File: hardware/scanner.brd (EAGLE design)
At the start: 65 x 56 mm, 24 parts, among them K1 PIN20X2, U1 CAT24C32WI-GT3, U2 TPS61165DBV

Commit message: update board layout
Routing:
- net +3V3: track 85.8 -> 63.3 mm
- net GND: track 21.2 -> 18.2 mm, vias 5 -> 6
- net N$1: track 32.3 -> 33.4 mm

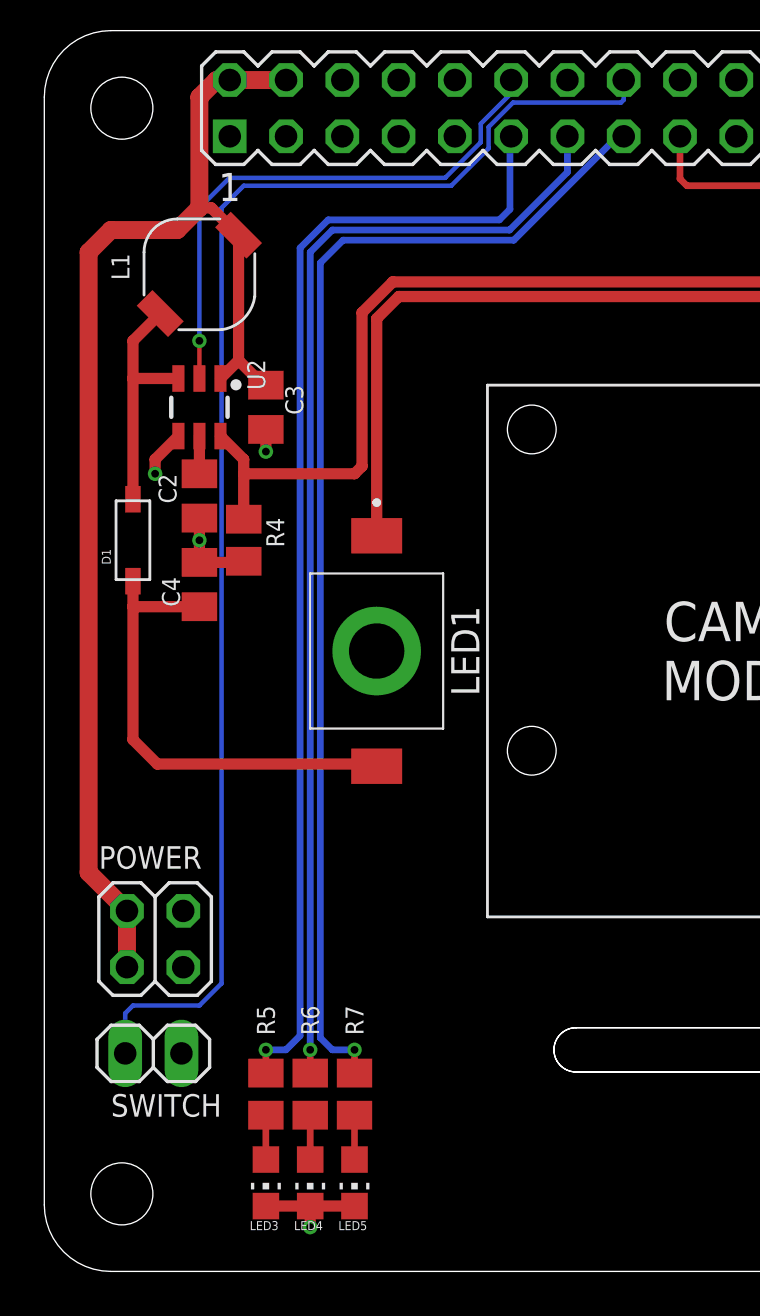
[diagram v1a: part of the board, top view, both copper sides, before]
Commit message: new power connector
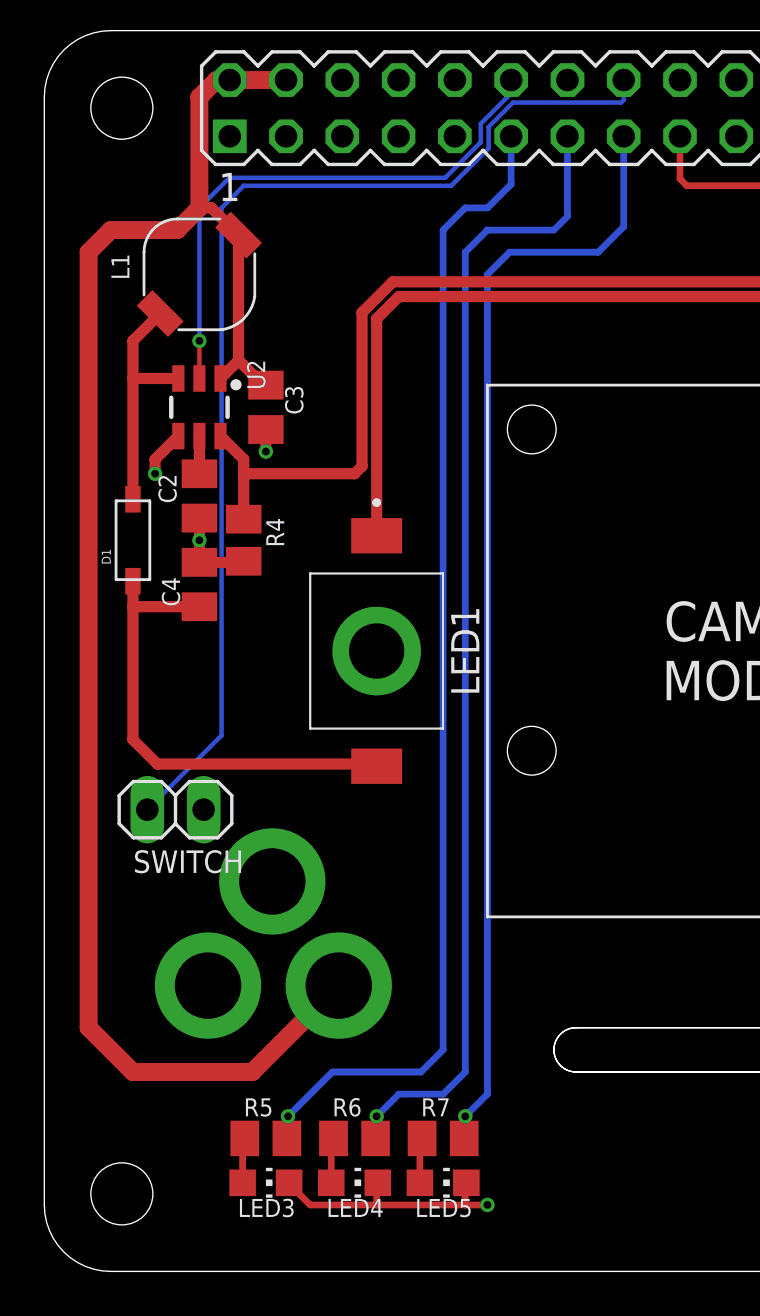
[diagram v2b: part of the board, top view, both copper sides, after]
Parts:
- POWER: value (none) -> 2.1MMJACKTHM; device pinhead:2X02 -> adafruit:PJ-102A
- moved SWITCH 11.0 mm to (5.92, 20.8)
- moved R7 4.47 mm to (18.0, 6.00), turned to 180 degrees
- moved LED5 4.00 mm to (18.0, 4.00), turned to 270 degrees
- moved R6 2.83 mm to (14.0, 6.00), turned to 180 degrees
- moved POWER 2.24 mm to (4.00, 13.0), flipped to the bottom, turned to 270 degrees
- moved LED4 2.00 mm to (14.0, 4.00), turned to 270 degrees
- moved R5 2.00 mm to (10.0, 6.00), turned to 180 degrees
- turned LED3 to 270 degrees
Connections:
- net +5V: now also POWER.TIP; no longer POWER.1, POWER.2
- net GND: now also POWER.RING, POWER.RING_SW; no longer POWER.3, POWER.4
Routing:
- net +5V: track 58.8 -> 74.6 mm
- net N$4: track 63.3 -> 50.2 mm
- net GND: track 18.2 -> 24.7 mm
- net N$20: track 53.9 -> 50.6 mm

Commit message: rename routes
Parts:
- removed SWITCH: (no value), pinhead:1X02
- added TRIGGER: (no value), pinhead:1X02
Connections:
- net N$1 renamed EEPROM_SDA
- net N$16 renamed LED4
- net N$19 renamed LED3
- net N$20 renamed LED5
- net N$3 renamed EEPROM_SCL
- net N$6 renamed EEPROM_WP
- removed net N$4: K1.16, SWITCH.2
- new net TRIGGER: K1.16, TRIGGER.2
- net GND: now also TRIGGER.1; no longer SWITCH.1
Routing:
- net TRIGGER: track 0.00 -> 50.8 mm
- net N$4: track 50.2 -> 0.00 mm
- net N$8: track 78.8 -> 78.1 mm
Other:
- board text added: "shopper.ink © Scanner HAT"
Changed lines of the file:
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@@
 <text x="32.635" y="28" size="1.778" layer="25" align="center">CAMERA
 MODULE</text>
+<text x="63" y="8" size="2.54" layer="25" rot="R90">shopper.ink ©
+Scanner HAT</text>
 </plain>
 <attributes>
@@
 </element>
 <element name="R1" library="resistor" package="M0805" value="3k9" x="61" y="39" smashed="yes" rot="R270">
-<attribute name="NAME" x="61" y="37" size="0.6096" layer="25" ratio="10" rot="R180" align="center"/>
+<attribute name="NAME" x="61" y="37" size="0.8128" layer="25" ratio="10" rot="R180" align="center"/>
 <attribute name="TOLERANCE" value="5%" x="61" y="39" size="1.778" layer="27" rot="R270" display="off"/>
 <attribute name="VALUE" x="59.984" y="37.1585" size="0.8128" layer="27" rot="R270"/>
@@
 </element>
 <element name="R2" library="resistor" package="M0805" value="3k9" x="59" y="39" smashed="yes" rot="R270">
-<attribute name="NAME" x="59" y="37" size="0.6096" layer="25" ratio="10" rot="R180" align="center"/>
+<attribute name="NAME" x="59" y="37" size="0.8128" layer="25" ratio="10" rot="R180" align="center"/>
 <attribute name="TOLERANCE" value="5%" x="59" y="39" size="1.778" layer="27" rot="R270" display="off"/>
 <attribute name="VALUE" x="57.984" y="37.1585" size="0.8128" layer="27" rot="R270"/>
 </element>
 <element name="U2" library="dword1511-pmic-dcdc" package="SOT-23-6" value="TPS61165DBV" x="7" y="39" smashed="yes" rot="R180">
-<attribute name="NAME" x="9.159" y="41.159" size="0.8128" layer="25" font="vector" rot="R270"/>
+<attribute name="NAME" x="5" y="40" size="0.8128" layer="25" font="vector" rot="R270" align="center-left"/>
 <attribute name="VALUE" x="4.2695" y="41.2225" size="0.8128" layer="27" font="vector" rot="R270"/>
 </element>
@@
 </element>
 <element name="R3" library="resistor" package="M0805" value="1k" x="57" y="39" smashed="yes" rot="R90">
-<attribute name="NAME" x="57" y="37" size="0.6096" layer="25" rot="R180" align="center"/>
+<attribute name="NAME" x="57" y="37" size="0.8128" layer="25" rot="R180" align="center"/>
 <attribute name="TOLERANCE" value="5%" x="57" y="39" size="1.778" layer="27" rot="R90" display="off"/>
 <attribute name="VALUE" x="59.286" y="37.984" size="1.27" layer="27" rot="R90"/>
 </element>
-<element name="SWITCH" library="pinhead" library_urn="urn:adsk.eagle:library:325" package="1X02" package3d_urn="urn:adsk.eagle:package:22435/2" value="" x="5.92" y="20.84" smashed="yes" rot="R180">
-<attribute name="NAME" x="9" y="19" size="1.016" layer="25" ratio="10" rot="R180"/>
-<attribute name="VALUE" x="8.46" y="24.015" size="1.27" layer="27" rot="R180"/>
+<element name="TRIGGER" library="pinhead" library_urn="urn:adsk.eagle:library:325" package="1X02" package3d_urn="urn:adsk.eagle:package:22435/2" value="" x="5.65" y="20.315" smashed="yes" rot="R180">
+<attribute name="NAME" x="8.73" y="18.475" size="1.016" layer="25" ratio="10" rot="R180"/>
+<attribute name="VALUE" x="8.19" y="23.49" size="1.27" layer="27" rot="R180"/>
 </element>
 <element name="JP1" library="pinhead" library_urn="urn:adsk.eagle:library:325" package="1X02" package3d_urn="urn:adsk.eagle:package:22435/2" value="" x="59" y="35" smashed="yes">
@@
 </element>
 <element name="D1" library="adafruit" library_urn="urn:adsk.eagle:library:420" package="SOD-123" package3d_urn="urn:adsk.eagle:package:6240753/1" value="40V 550mA" x="4" y="33" smashed="yes" rot="R90">
-<attribute name="NAME" x="3" y="31.9" size="0.4064" layer="25" rot="R90"/>
+<attribute name="NAME" x="3" y="31.9" size="0.8128" layer="25" rot="R90"/>
 <attribute name="VALUE" x="5.284" y="31.9" size="0.4064" layer="27" rot="R90"/>
 </element>
@@
 <contactref element="U1" pad="1"/>
 <contactref element="U1" pad="2"/>
-<contactref element="SWITCH" pad="1"/>
+<contactref element="TRIGGER" pad="1"/>
 <contactref element="JP1" pad="2"/>
 <polygon width="0.1524" layer="2">
@@
 <wire x1="8.37" y1="51.23" x2="28.69" y2="51.23" width="0" layer="19" extent="1-1"/>
 </signal>
-<signal name="N$1">
+<signal name="EEPROM_SDA">
 <contactref element="R1" pad="1"/>
 <contactref element="K1" pad="28"/>
@@
 <wire x1="2" y1="11" x2="2" y2="46" width="0.8128" layer="1"/>
 </signal>
-<signal name="N$4">
+<signal name="TRIGGER">
 <contactref element="K1" pad="16"/>
-<contactref element="SWITCH" pad="2"/>
+<contactref element="TRIGGER" pad="2"/>
 <wire x1="8" y1="48" x2="9" y2="49" width="0.2032" layer="16"/>
 <wire x1="9" y1="49" x2="18.365" y2="49" width="0.2032" layer="16"/>
@@
 <wire x1="20.054" y1="51.65084375" x2="21.15715625" y2="52.754" width="0.2032" layer="16"/>
 <wire x1="21.15715625" y1="52.754" x2="26.03084375" y2="52.754" width="0.2032" layer="16"/>
-<wire x1="4.65" y1="20.84" x2="8" y2="24.19" width="0.2032" layer="16"/>
-<wire x1="8" y1="24.19" x2="8" y2="48" width="0.2032" layer="16"/>
+<wire x1="4.38" y1="20.315" x2="8" y2="23.935" width="0.2032" layer="16"/>
+<wire x1="8" y1="23.935" x2="8" y2="48" width="0.2032" layer="16"/>
 </signal>
 <signal name="N$5">
@@
 <wire x1="8.3556" y1="49.3556" x2="18.09244375" y2="49.3556" width="0.2032" layer="16"/>
 </signal>
-<signal name="N$6">
+<signal name="EEPROM_WP">
 <contactref element="U1" pad="7"/>
 <contactref element="JP1" pad="1"/>
@@
 <via x="58" y="42" extent="1-16" drill="0.35"/>
 </signal>
-<signal name="N$3">
+<signal name="EEPROM_SCL">
 <contactref element="R2" pad="1"/>
 <contactref element="U1" pad="6"/>
@@
 <contactref element="LED2" pad="1"/>
 <wire x1="7.95" y1="37.6999" x2="8" y2="37.6499" width="0.508" layer="1"/>
+<wire x1="9" y1="36.6499" x2="9" y2="36" width="0.508" layer="1"/>
 <wire x1="9" y1="36" x2="9" y2="33.95" width="0.508" layer="1"/>
-<wire x1="9" y1="36" x2="14" y2="36" width="0.508" layer="1"/>
-<wire x1="14" y1="36" x2="14.3396" y2="36.3396" width="0.508" layer="1"/>
-<wire x1="15.72645" y1="44.6604" x2="49.27355" y2="44.6604" width="0.508" layer="1"/>
-<wire x1="14.3396" y1="36.3396" x2="14.3396" y2="43.27355" width="0.508" layer="1"/>
-<wire x1="14.3396" y1="43.27355" x2="15.72645" y2="44.6604" width="0.508" layer="1"/>
-<wire x1="49.27355" y1="44.6604" x2="50.6604" y2="43.27355" width="0.508" layer="1"/>
-<wire x1="50.6604" y1="34.746" x2="51" y2="34.4064" width="0.508" layer="1"/>
-<wire x1="50.6604" y1="43.27355" x2="50.6604" y2="34.746" width="0.508" layer="1"/>
-<wire x1="51" y1="34.4064" x2="52.5936" y2="34.4064" width="0.508" layer="1"/>
-<wire x1="52.5936" y1="34.4064" x2="53" y2="34" width="0.508" layer="1"/>
-<wire x1="53" y1="34" x2="53" y2="24" width="0.508" layer="1"/>
+<wire x1="15.69" y1="45" x2="49.385" y2="45" width="0.508" layer="1"/>
+<wire x1="14" y1="43.31" x2="14" y2="37" width="0.508" layer="1"/>
+<wire x1="14" y1="43.31" x2="15.69" y2="45" width="0.508" layer="1"/>
+<wire x1="49.385" y1="45" x2="51" y2="43.385" width="0.508" layer="1"/>
+<wire x1="51" y1="35.4064" x2="53" y2="33.4064" width="0.508" layer="1"/>
+<wire x1="51" y1="43.385" x2="51" y2="35.4064" width="0.508" layer="1"/>
+<wire x1="53" y1="33.4064" x2="53" y2="24" width="0.508" layer="1"/>
 <wire x1="51.8" y1="22.8" x2="50" y2="22.8" width="0.508" layer="1"/>
 <wire x1="53" y1="24" x2="51.8" y2="22.8" width="0.508" layer="1"/>
 <wire x1="7.95" y1="37.6999" x2="9" y2="36.6499" width="0.508" layer="1"/>
-<wire x1="9" y1="36.6499" x2="9" y2="36" width="0.508" layer="1"/>
+<wire x1="14" y1="37" x2="13" y2="36" width="0.508" layer="1"/>
+<wire x1="13" y1="36" x2="9" y2="36" width="0.508" layer="1"/>
 </signal>
 <signal name="N$9">
@@
 <wire x1="16.95" y1="5.9" x2="16.95" y2="4" width="0.3048" layer="1"/>
 </signal>
-<signal name="N$16">
+<signal name="LED4">
 <contactref element="K1" pad="13"/>
 <contactref element="R6" pad="1"/>
@@
 <wire x1="19" y1="9" x2="19" y2="46" width="0.3048" layer="16"/>
 </signal>
-<signal name="N$19">
+<signal name="LED3">
 <contactref element="K1" pad="11"/>
 <contactref element="R5" pad="1"/>
@@
 <wire x1="18" y1="10" x2="18" y2="47" width="0.3048" layer="16"/>
 </signal>
-<signal name="N$20">
+<signal name="LED5">
 <contactref element="K1" pad="15"/>
 <contactref element="R7" pad="1"/>

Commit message: update text
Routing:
- net N$10: track 21.8 -> 20.5 mm
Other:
- board text added: "Scanner HAT"
- board text added: "shopper.ink © v1.0"
- board text removed: "shopper.ink © Scanner HAT"
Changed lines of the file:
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@@
 <text x="32.635" y="28" size="1.778" layer="25" align="center">CAMERA
 MODULE</text>
-<text x="63" y="8" size="2.54" layer="25" rot="R90">shopper.ink ©
-Scanner HAT</text>
+<text x="61" y="8" size="2.54" layer="25" rot="R90">Scanner HAT</text>
+<text x="62" y="8" size="0.8128" layer="25" rot="R90" align="center-left">shopper.ink ©    v1.0</text>
+<circle x="3.5" y="52.5" radius="1.55" width="3.1" layer="42"/>
 </plain>
 <attributes>
@@
 <wire x1="9" y1="36" x2="9" y2="33.95" width="0.508" layer="1"/>
 <wire x1="15.69" y1="45" x2="49.385" y2="45" width="0.508" layer="1"/>
-<wire x1="14" y1="43.31" x2="14" y2="37" width="0.508" layer="1"/>
+<wire x1="14" y1="43.31" x2="14" y2="43" width="0.508" layer="1"/>
+<wire x1="14" y1="43" x2="14" y2="37" width="0.508" layer="1"/>
 <wire x1="14" y1="43.31" x2="15.69" y2="45" width="0.508" layer="1"/>
 <wire x1="49.385" y1="45" x2="51" y2="43.385" width="0.508" layer="1"/>
@@
 <wire x1="4" y1="31.15" x2="4" y2="30" width="0.508" layer="1"/>
 <wire x1="7" y1="30" x2="4" y2="30" width="0.508" layer="1"/>
-<wire x1="4" y1="30" x2="4" y2="24" width="0.508" layer="1"/>
-<wire x1="14.8" y1="23" x2="14.9" y2="22.9" width="0.508" layer="1"/>
-<wire x1="14.9" y1="22.9" x2="15" y2="22.8" width="0.508" layer="1"/>
-<wire x1="4" y1="24" x2="5.1" y2="22.9" width="0.508" layer="1"/>
-<wire x1="5.1" y1="22.9" x2="14.9" y2="22.9" width="0.508" layer="1"/>
+<wire x1="4" y1="30" x2="4" y2="29" width="0.508" layer="1"/>
+<wire x1="4" y1="29" x2="5" y2="28" width="0.508" layer="1"/>
+<wire x1="5" y1="28" x2="11" y2="28" width="0.508" layer="1"/>
+<wire x1="12" y1="27" x2="11" y2="28" width="0.508" layer="1"/>
+<wire x1="15" y1="22.8" x2="13.2" y2="22.8" width="0.508" layer="1"/>
+<wire x1="13.2" y1="22.8" x2="12" y2="24" width="0.508" layer="1"/>
+<wire x1="12" y1="24" x2="12" y2="27" width="0.508" layer="1"/>
 </signal>
 <signal name="N$11">

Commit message: added proper sensor connector
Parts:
- added R8: 10k, resistor:M0805
- R7: value 330 -> 10k
- TRIGGER: value (none) -> 22-05-7038-03; device pinhead:1X02 -> con-molex:7395-03
- moved TRIGGER 2.76 mm to (5.00, 23.0), turned to 270 degrees
- moved POWER 2.00 mm to (2.00, 13.0)
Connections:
- net +5V: now also R8.2, TRIGGER.1
- net GND: now also TRIGGER.2; no longer TRIGGER.1
- net TRIGGER: now also R8.1, TRIGGER.3; no longer TRIGGER.2
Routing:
- net +5V: track 74.6 -> 82.6 mm
- net TRIGGER: track 50.8 -> 52.5 mm
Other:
- board text added: "+5V"
- board text added: "CTRL"
- board text added: "GND"
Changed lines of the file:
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@@
 <text x="62" y="8" size="0.8128" layer="25" rot="R90" align="center-left">shopper.ink ©    v1.0</text>
 <circle x="3.5" y="52.5" radius="1.55" width="3.1" layer="42"/>
+<text x="8" y="23" size="0.8128" layer="25" rot="R180" align="center">GND</text>
+<text x="7.605" y="20.545" size="0.8128" layer="25" align="center">+5V</text>
+<text x="8" y="25.635" size="0.8128" layer="25" rot="R180" align="center">CTRL</text>
 </plain>
 <attributes>
@@
 <attribute name="VALUE" x="59.286" y="37.984" size="1.27" layer="27" rot="R90"/>
 </element>
-<element name="TRIGGER" library="pinhead" library_urn="urn:adsk.eagle:library:325" package="1X02" package3d_urn="urn:adsk.eagle:package:22435/2" value="" x="5.65" y="20.315" smashed="yes" rot="R180">
-<attribute name="NAME" x="8.73" y="18.475" size="1.016" layer="25" ratio="10" rot="R180"/>
-<attribute name="VALUE" x="8.19" y="23.49" size="1.27" layer="27" rot="R180"/>
-</element>
 <element name="JP1" library="pinhead" library_urn="urn:adsk.eagle:library:325" package="1X02" package3d_urn="urn:adsk.eagle:package:22435/2" value="" x="59" y="35" smashed="yes">
 <attribute name="NAME" x="56" y="36" size="0.8128" layer="25" ratio="10" rot="R90" align="bottom-right"/>
@@
 <attribute name="VALUE" x="16.73" y="1.46" size="1.27" layer="27"/>
 </element>
-<element name="R7" library="resistor" package="M0805" value="330" x="18" y="6" smashed="yes" rot="R180">
+<element name="R7" library="resistor" package="M0805" value="10k" x="18" y="6" smashed="yes" rot="R180">
 <attribute name="NAME" x="17" y="7" size="0.8128" layer="25" rot="R180" align="top-right"/>
 <attribute name="TOLERANCE" value="5%" x="25" y="6" size="1.778" layer="27" rot="R180" display="off"/>
 <attribute name="VALUE" x="19.016" y="8.286" size="1.27" layer="27" rot="R180"/>
 </element>
-<element name="POWER" library="adafruit" library_urn="urn:adsk.eagle:library:420" package="PJ-102A" package3d_urn="urn:adsk.eagle:package:6240341/1" value="2.1MMJACKTHM" x="4" y="13" smashed="yes" rot="MR270"/>
+<element name="POWER" library="adafruit" library_urn="urn:adsk.eagle:library:420" package="PJ-102A" package3d_urn="urn:adsk.eagle:package:6240341/1" value="2.1MMJACKTHM" x="2" y="13" smashed="yes" rot="MR270"/>
+<element name="TRIGGER" library="con-molex" library_urn="urn:adsk.eagle:library:165" package="7395-03" value="22-05-7038-03" x="5" y="23" smashed="yes" rot="R270">
+<attribute name="MF" value="MOLEX" x="5" y="23" size="1.778" layer="27" rot="R270" display="off"/>
+<attribute name="MPN" value="" x="5" y="23" size="1.778" layer="27" rot="R270" display="off"/>
+<attribute name="NAME" x="1" y="23" size="1.016" layer="25" ratio="10" rot="R270" align="center"/>
+<attribute name="OC_FARNELL" value="unknown" x="5" y="23" size="1.778" layer="27" rot="R270" display="off"/>
+<attribute name="OC_NEWARK" value="unknown" x="5" y="23" size="1.778" layer="27" rot="R270" display="off"/>
+<attribute name="VALUE" x="2.5601" y="18.3279" size="0.8128" layer="27" ratio="10" rot="R180"/>
+</element>
+<element name="R8" library="resistor" package="M0805" value="10k" x="10" y="23" smashed="yes" rot="R270">
+<attribute name="NAME" x="10.016" y="26.016" size="0.8128" layer="25" rot="R270" align="center-left"/>
+<attribute name="TOLERANCE" value="5%" x="10" y="23" size="1.778" layer="27" rot="R270" display="off"/>
+<attribute name="VALUE" x="7.714" y="24.016" size="1.27" layer="27" rot="R270"/>
+</element>
 </elements>
 <signals>
@@
 <contactref element="U1" pad="1"/>
 <contactref element="U1" pad="2"/>
-<contactref element="TRIGGER" pad="1"/>
 <contactref element="JP1" pad="2"/>
 <polygon width="0.1524" layer="2">
@@
 <wire x1="19" y1="3" x2="19" y2="3.95" width="0.3048" layer="1"/>
 <wire x1="19" y1="3.95" x2="19.05" y2="4" width="0.3048" layer="1"/>
+<contactref element="TRIGGER" pad="2"/>
 </signal>
 <signal name="+3V3">
@@
 <wire x1="7.53553125" y1="48" x2="7" y2="48" width="0.508" layer="1"/>
 <contactref element="POWER" pad="TIP"/>
-<wire x1="13.29" y1="12.9" x2="9.39" y2="9" width="0.8128" layer="1"/>
+<wire x1="11.29" y1="12.9" x2="11.29" y2="10.9" width="0.8128" layer="1"/>
+<wire x1="11.29" y1="10.9" x2="9.39" y2="9" width="0.8128" layer="1"/>
 <wire x1="9.39" y1="9" x2="4" y2="9" width="0.8128" layer="1"/>
 <wire x1="4" y1="9" x2="2" y2="11" width="0.8128" layer="1"/>
-<wire x1="2" y1="11" x2="2" y2="46" width="0.8128" layer="1"/>
+<contactref element="TRIGGER" pad="1"/>
+<wire x1="2" y1="11" x2="2" y2="21" width="0.8128" layer="1"/>
+<wire x1="2" y1="21" x2="2" y2="46" width="0.8128" layer="1"/>
+<wire x1="5" y1="20.46" x2="4.46" y2="21" width="0.508" layer="1"/>
+<wire x1="4.46" y1="21" x2="2" y2="21" width="0.508" layer="1"/>
+<contactref element="R8" pad="2"/>
+<wire x1="9.41" y1="21.46" x2="6" y2="21.46" width="0.508" layer="1"/>
+<wire x1="5" y1="20.46" x2="6" y2="21.46" width="0.508" layer="1"/>
+<wire x1="9.41" y1="21.46" x2="10" y2="22.05" width="0.508" layer="1"/>
 </signal>
 <signal name="TRIGGER">
 <contactref element="K1" pad="16"/>
-<contactref element="TRIGGER" pad="2"/>
 <wire x1="8" y1="48" x2="9" y2="49" width="0.2032" layer="16"/>
 <wire x1="9" y1="49" x2="18.365" y2="49" width="0.2032" layer="16"/>
@@
 <wire x1="20.054" y1="51.65084375" x2="21.15715625" y2="52.754" width="0.2032" layer="16"/>
 <wire x1="21.15715625" y1="52.754" x2="26.03084375" y2="52.754" width="0.2032" layer="16"/>
-<wire x1="4.38" y1="20.315" x2="8" y2="23.935" width="0.2032" layer="16"/>
-<wire x1="8" y1="23.935" x2="8" y2="48" width="0.2032" layer="16"/>
+<contactref element="TRIGGER" pad="3"/>
+<wire x1="8" y1="26" x2="8" y2="48" width="0.2032" layer="16"/>
+<wire x1="5" y1="25.54" x2="7.54" y2="25.54" width="0.2032" layer="16"/>
+<wire x1="7.54" y1="25.54" x2="8" y2="26" width="0.2032" layer="16"/>
+<contactref element="R8" pad="1"/>
+<wire x1="10" y1="23.95" x2="9.41" y2="24.54" width="0.508" layer="1"/>
+<wire x1="9.41" y1="24.54" x2="6" y2="24.54" width="0.508" layer="1"/>
+<wire x1="6" y1="24.54" x2="5" y2="25.54" width="0.508" layer="1"/>
 </signal>
 <signal name="N$5">
